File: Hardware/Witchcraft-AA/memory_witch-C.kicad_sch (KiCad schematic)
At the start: 3 parts, among them U1 Z1 extreme, U3 K3LKCKC0BM, U4 K3LKCKC0BM

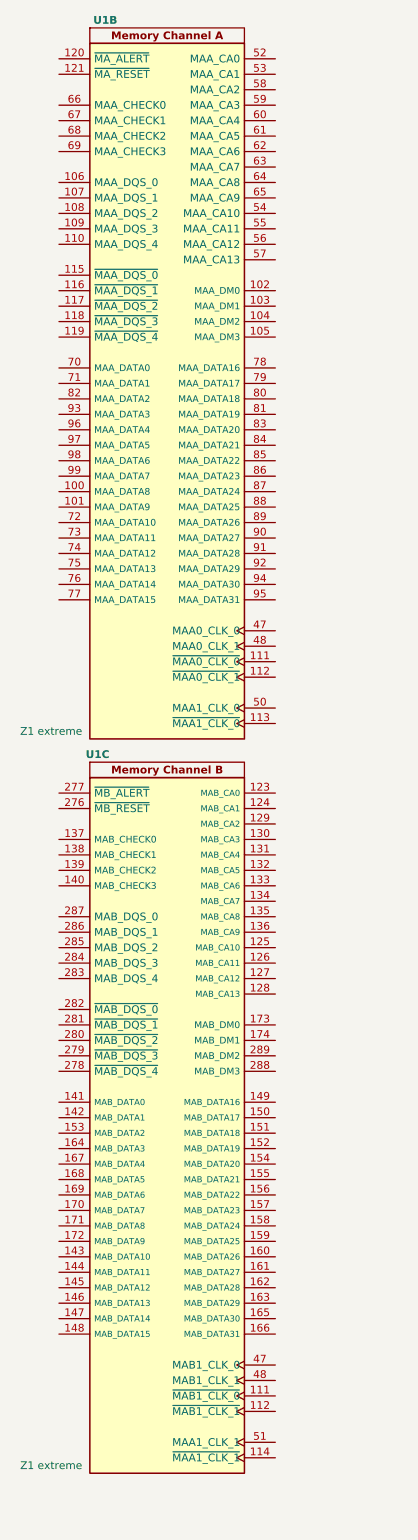
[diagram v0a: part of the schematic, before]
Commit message: ECAD: replaced the Z1 Extreme with the 7840U chip, as the AI-engine will be more useful for makers and non-gamers. MCAD: continued converting the outer shell towards a Assembly4-architecture, adding more items. Started a big change in design wherein I'm splitting the shell-design into a modular one, to accomodate removable controllers. Made some minor tweaks to the cooling-assembly, to accomodate the new, split shell-design. Updated the Readme to describe the project.
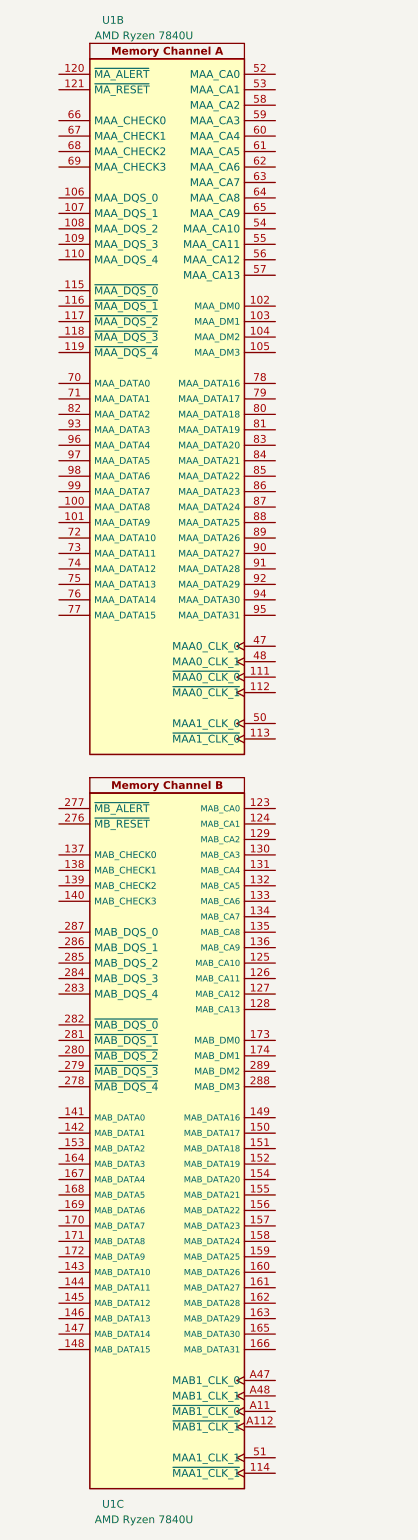
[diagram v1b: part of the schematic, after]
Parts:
- U1: value Z1 extreme -> AMD Ryzen 7840U; symbol LRJ-parts:AMD_Z1_extreme -> LRJ-parts:AMD_Ryzen_7840U_FP8; Details https://en.wikichip.org/wiki/amd/packages/socket_am5#Packag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 -> https://en.wikichip.org/wiki/amd/packages/fp6; Operating temperature (none) -> 0 C ~ 45 C
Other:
- moved on the sheet: U1B, U1C

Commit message: MCAD: Added Oculink connector. ECAD: Added Oculink connector.
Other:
- title: (none) -> WITCHCRAFT HANDHELD
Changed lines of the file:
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@@
   (paper "A3")
   (title_block
+    (title "WITCHCRAFT HANDHELD")
     (date "2023-05-06")
     (rev "A-A")
